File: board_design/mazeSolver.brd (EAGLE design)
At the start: 130 x 130 mm, 53 parts, among them IC1 L293DD, IC2 7805TV, IC3 CP2101, Q1 BC547, Q2 BC547, U1 MPU-9250, U2 AP1509-SOP8L, U3 ESP-WROOM-32, U4 GY-521MPU6050, U5 RST, U6 BOOT

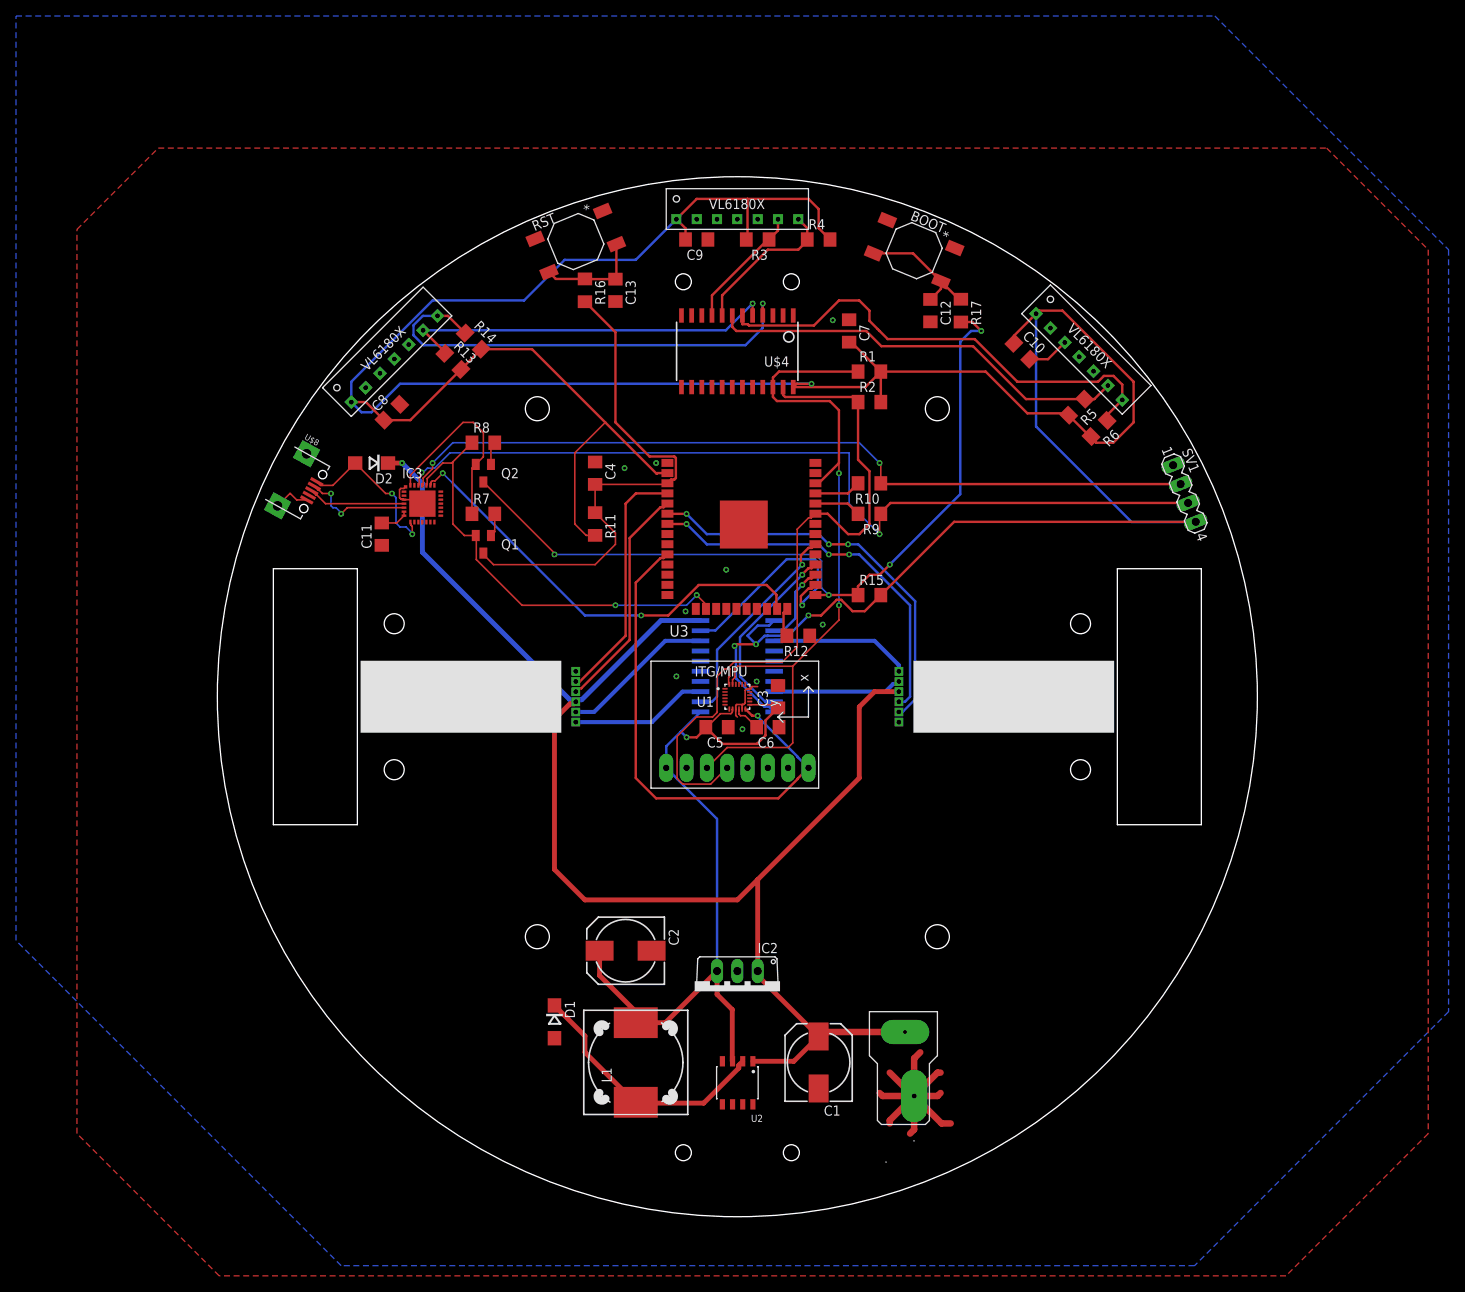
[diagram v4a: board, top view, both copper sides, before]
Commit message: DRC Checks are passing
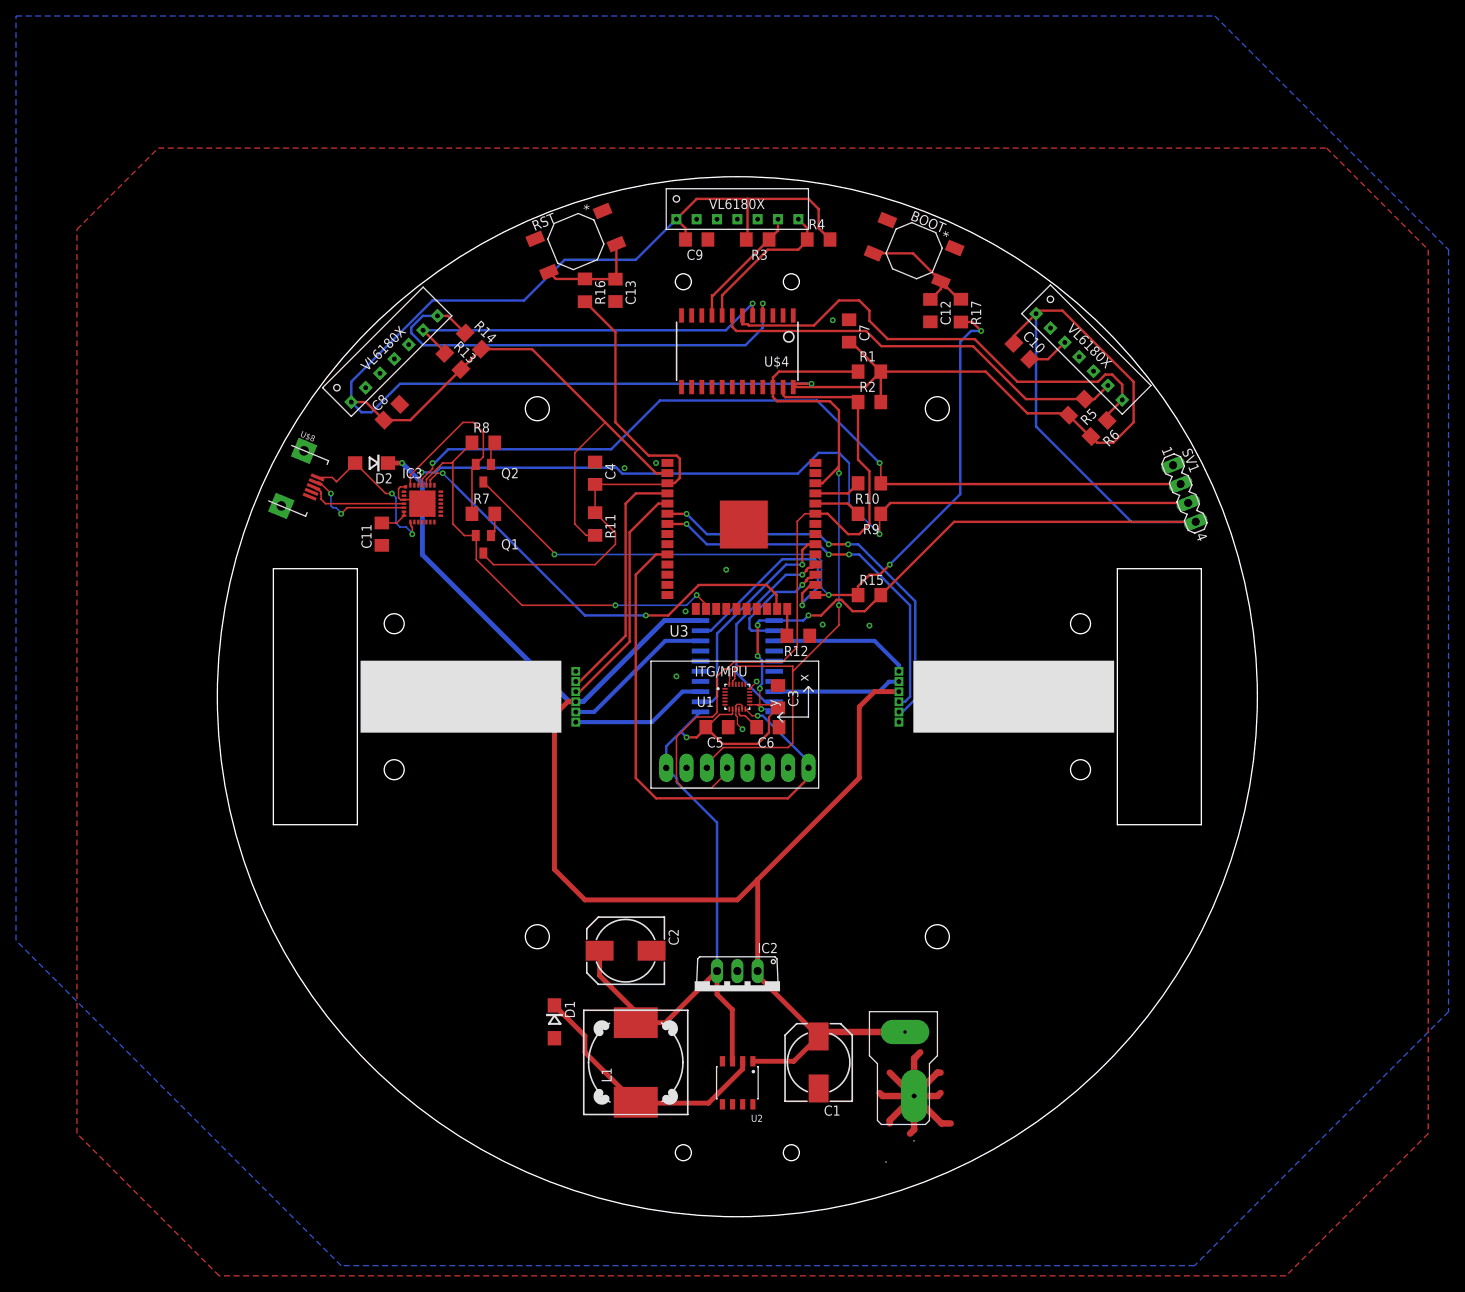
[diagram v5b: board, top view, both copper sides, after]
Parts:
- turned U$8 to 247.5 degrees
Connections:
- removed net DSR: IC3.27
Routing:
- net +3V3: track 519.9 -> 511.7 mm, vias 5 -> 7
- net INA1: track 10.2 -> 15.5 mm
- net GND: track 59.8 -> 54.6 mm
- net RXD: track 101.4 -> 105.8 mm
- net INA2: track 23.9 -> 25.9 mm
- net INT: track 65.1 -> 66.8 mm
- net SDA: track 90.0 -> 91.6 mm
- net INB1: track 27.0 -> 28.2 mm
- net EN: track 65.8 -> 66.7 mm
- net SCL: track 91.8 -> 92.5 mm
- net N$16: track 3.97 -> 3.37 mm
- net ENCB1: track 28.7 -> 29.2 mm
- net VCC: track 187.5 -> 188.0 mm
